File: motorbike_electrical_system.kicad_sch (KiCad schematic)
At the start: 94 parts, among them IC1 BDX34C, IC2 BDX34C, IC3 BDX34C, IC4 BDX34C, IC5 BDX34C, IC6 BDX34C, U1 L7805, U2 L7805, U3 L7805

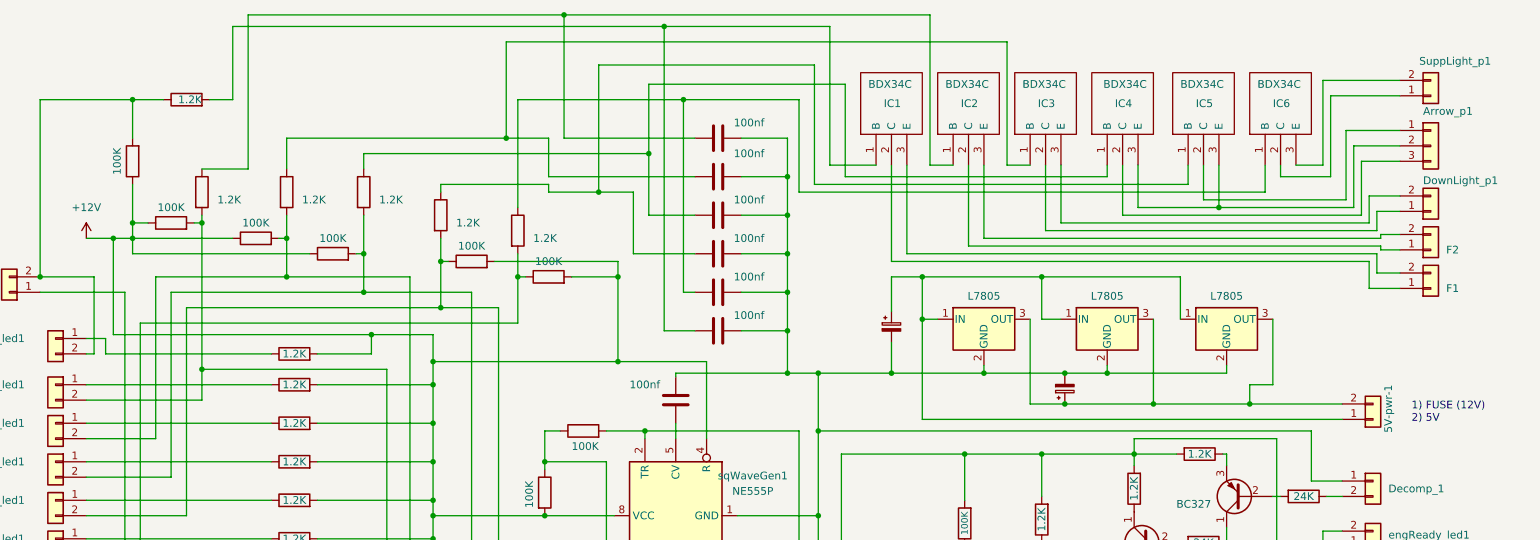
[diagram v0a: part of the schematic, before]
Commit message: enhancement: BDX34C replaced by D45VH10
In order to reduce the wasted electric power BDX34C (VCE=2.5V) has been replaced by D45VH10 (VCE=0.3V) for up-light and added-light
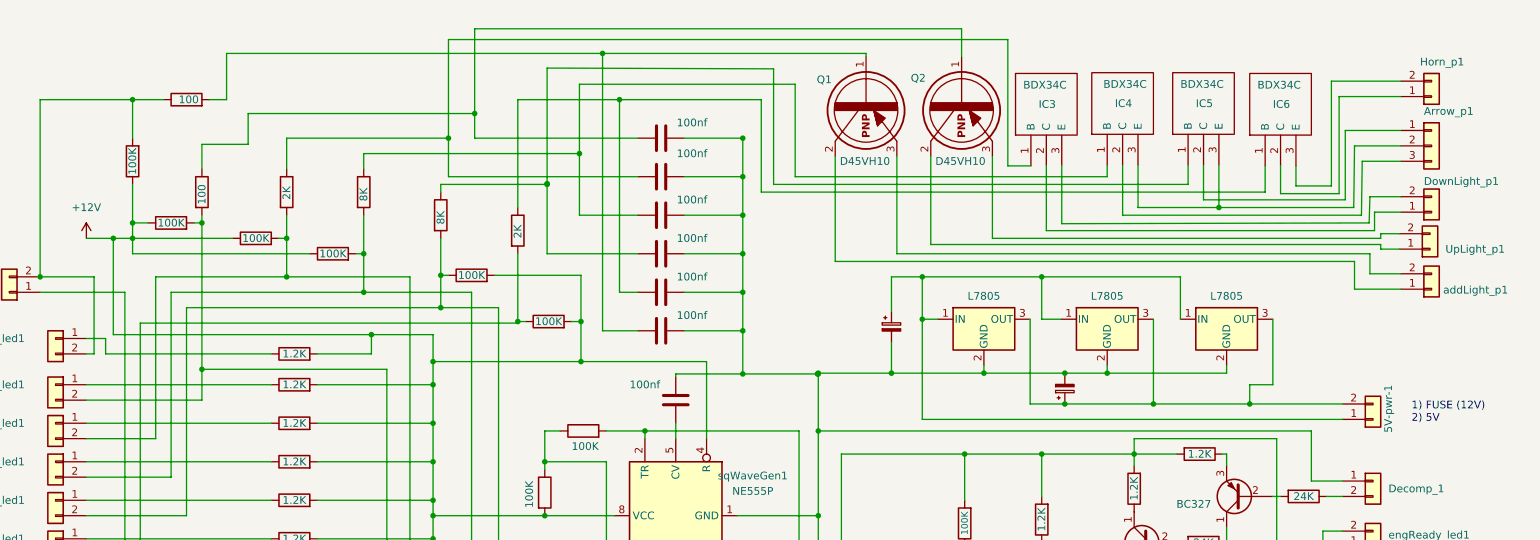
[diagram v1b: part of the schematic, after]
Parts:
- removed IC1, IC2: BDX34C, BDX34C:TO270P460X1020X2008-3P, symbol BDX34C:BDX34C
- added Q1, Q2: D45VH10, Package_TO_SOT_THT:TO-220-3_Vertical, symbol D45VH10:D45VH10
- BT5, RB1, RB2, RB3, RBT2, RBT3, RBT4, RC1, RC2: footprint Resistor_THT:R_Axial_DIN0207_L6.3mm_D2.5mm_P7.62mm_Horizontal -> Resistor_THT:R_Axial_DIN0204_L3.6mm_D1.6mm_P5.08mm_Horizontal
- RBT1, RBT6: footprint Resistor_THT:R_Axial_DIN0207_L6.3mm_D2.5mm_P7.62mm_Horizontal -> Resistor_THT:R_Axial_DIN0204_L3.6mm_D1.6mm_P7.62mm_Horizontal
- RTA1, RTA6: value 1.2K -> 100; footprint Resistor_THT:R_Axial_DIN0207_L6.3mm_D2.5mm_P7.62mm_Horizontal -> Resistor_THT:R_Axial_DIN0516_L15.5mm_D5.0mm_P20.32mm_Horizontal
- RTA2, RTA5: value 1.2K -> 2K
- RTA3, RTA4: value 1.2K -> 8K; footprint Resistor_THT:R_Axial_DIN0207_L6.3mm_D2.5mm_P7.62mm_Horizontal -> Resistor_THT:R_Axial_DIN0204_L3.6mm_D1.6mm_P7.62mm_Horizontal
- renumbered SuppLight_p1 to Horn_p1, F2 to UpLight_p1, F1 to addLight_p1
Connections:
- net at C8.1, RTA6.2: now also Q1.1
- net at C3.1, RTA1.1: now also Q2.1
- net at UpLight_p1.1 (Pin_1): now also Q2.2
- net at UpLight_p1.2 (Pin_2): now also Q2.3
- net at addLight_p1.1 (Pin_1): now also Q1.2
- net at addLight_p1.2 (Pin_2): now also Q1.3

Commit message: First release of all-in-one solution
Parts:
- removed 12V-keyON1, Batt_12V1: Conn_01x01, Connector_Wire:SolderWire-0.5sqmm_1x01_D0.9mm_OD2.1mm, symbol Connector_Generic:Conn_01x01
- removed 5V-pwr-1, DownLight_p1, Horn_p1, UpLight_p1, addLight_p1: Conn_01x02, Connector_Wire:SolderWire-1.5sqmm_1x02_P6mm_D1.7mm_OD3mm, symbol Connector_Generic:Conn_01x02
- removed Arrow_p1: Conn_01x03, Connector_Wire:SolderWire-1.5sqmm_1x03_P6mm_D1.7mm_OD3mm, symbol Connector_Generic:Conn_01x03
- removed BT5, RB1, RB2, RB3, RBT2, RBT3, RBT4, RC1, RC2: 100K, Resistor_THT:R_Axial_DIN0204_L3.6mm_D1.6mm_P5.08mm_Horizontal, symbol Device:R
- removed Batt_GND1: Conn_01x01, Connector_Wire:SolderWire-1.5sqmm_1x01_D1.7mm_OD3.9mm, symbol Connector_Generic:Conn_01x01
- removed Bike_stand1, Decomp_1, Decomp_disabl_1, LightOnOff_sw1, addLights1: Conn_01x02, Connector_PinSocket_2.54mm:PinSocket_1x02_P2.54mm_Vertical, symbol Connector_Generic:Conn_01x02
- removed C1: 1uF, Capacitor_THT:CP_Radial_D6.3mm_P2.50mm, symbol Device:C
- removed C10: C_Polarized_Small, Capacitor_THT:CP_Radial_D8.0mm_P2.50mm, symbol Device:C_Polarized_Small
- removed C11, C12, C13: 50uF, Capacitor_THT:CP_Radial_D6.3mm_P2.50mm, symbol Device:C
- removed C2, C3, C4, C5, C6, C7, C8: 100nf, Capacitor_THT:C_Disc_D6.0mm_W4.4mm_P5.00mm, symbol Device:C
- removed DC1: BC327, Package_TO_SOT_THT:TO-92_Inline_Wide, symbol Transistor_BJT:BC327
- removed DC2, DC3, DC4, DC5, Q_arr1, Q_arr2: BC337, Package_TO_SOT_THT:TO-92_Inline_Wide, symbol Transistor_BJT:BC337
- removed ElectronicKey1: Conn_01x03, Connector_PinHeader_2.54mm:PinHeader_1x03_P2.54mm_Vertical, symbol Connector_Generic:Conn_01x03
- removed GND-faston1: Conn_01x01, Connector_Wire:SolderWire-0.75sqmm_1x01_D1.25mm_OD2.3mm, symbol Connector_Generic:Conn_01x01
- removed GND2DEVS1: Conn_01x06, Connector_Wire:SolderWire-1sqmm_1x06_P7.8mm_D1.4mm_OD3.9mm, symbol Connector_Generic:Conn_01x06
- removed IC3, IC4, IC5, IC6: BDX34C, BDX34C:TO270P460X1020X2008-3P, symbol BDX34C:BDX34C
- removed Q1, Q2: D45VH10, Package_TO_SOT_THT:TO-220-3_Vertical, symbol D45VH10:D45VH10
- removed RA1, RA2, RE1: 5K, Resistor_THT:R_Axial_DIN0207_L6.3mm_D2.5mm_P7.62mm_Horizontal, symbol Device:R
- removed RA3, RA5: 12K, Resistor_THT:R_Axial_DIN0207_L6.3mm_D2.5mm_P7.62mm_Horizontal, symbol Device:R
- removed RA4, RA6, RA8: 24K, Resistor_THT:R_Axial_DIN0207_L6.3mm_D2.5mm_P7.62mm_Horizontal, symbol Device:R
- removed RA7, RL1, RL10, RL2, RL3, RL4, RL5, RL6, RL7, RL8, RL9: 1.2K, Resistor_THT:R_Axial_DIN0207_L6.3mm_D2.5mm_P7.62mm_Horizontal, symbol Device:R
- removed RBT1, RBT6: 100K, Resistor_THT:R_Axial_DIN0204_L3.6mm_D1.6mm_P7.62mm_Horizontal, symbol Device:R
- removed RTA1, RTA6: 100, Resistor_THT:R_Axial_DIN0516_L15.5mm_D5.0mm_P20.32mm_Horizontal, symbol Device:R
- removed RTA2, RTA5: 2K, Resistor_THT:R_Axial_DIN0207_L6.3mm_D2.5mm_P7.62mm_Horizontal, symbol Device:R
- removed RTA3, RTA4: 8K, Resistor_THT:R_Axial_DIN0204_L3.6mm_D1.6mm_P7.62mm_Horizontal, symbol Device:R
- removed RearDevs1: Conn_01x09, Connector_PinHeader_2.54mm:PinHeader_1x09_P2.54mm_Vertical, symbol Connector_Generic:Conn_01x09
- removed addLight_led1, downLight_led1, engReady_led1, engineON_led1, leftArrow_led1, neutralG_led1, rightArrow_led1, upLight_led1: Conn_01x02, Connector_JST:JST_XH_B2B-XH-AM_1x02_P2.50mm_Vertical, symbol Connector_Generic:Conn_01x02
- removed lerftCtrls_conn1, rightCtrls_conn1: Conn_01x06, Connector_PinHeader_2.54mm:PinHeader_1x06_P2.54mm_Vertical, symbol Connector_Generic:Conn_01x06
- removed sqWaveGen1: NE555P, Package_DIP:DIP-8_W7.62mm, symbol Timer:NE555P
- added Battery1: Conn_01x02, Connector_Wire:SolderWire-0.75sqmm_1x02_P7mm_D1.25mm_OD3.5mm, symbol Connector_Generic:Conn_01x02
- added U4: ATmega16L-8P, Package_DIP:DIP-40_W15.24mm, symbol ATmega:ATmega16L-8P
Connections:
- net +12V: now also C9.1, U1.1 (IN), U2.1 (IN), U3.1 (IN), Battery1.1 (Pin_1)
- net GND: now also Battery1.2 (Pin_2), U4.11 (GND), U4.31 (GND)
- net +5V: now reaches U1.3 (OUT), U2.3 (OUT), U3.3 (OUT)
- new net i_Vx1: U4.40 (PA0)
- new net i_Vx2: U4.39 (PA1)
- new net i_addLight: U4.28 (PC6)
- new net i_brakeSwitch: U4.22 (PC0), U4.34 (PA6)
- new net i_bykeStand: U4.6 (PB5)
- new net i_decompr: U4.25 (PC3)
- new net i_downLight: U4.2 (PB1)
- new net i_engineON: U4.24 (PC2)
- new net i_horn: U4.5 (PB4)
- new net i_leftArrow: U4.1 (PB0)
- new net i_lightON/OFF: U4.29 (PC7)
- new net i_neutral: U4.33 (PA7)
- new net i_rightArrow: U4.4 (PB3)
- new net i_startButton: U4.23 (PC1)
- new net i_upLight: U4.3 (PB2)
- new net o_addLight: U4.18 (PD4)
- new net o_downLight: U4.16 (PD2)
- new net o_engineReady: U4.7 (PB6)
- new net o_horn: U4.19 (PD5)
- new net o_keepAlive: U4.20 (PD6)
- new net o_leftArrow: U4.15 (PD1)
- new net o_neutral: U4.8 (PB7)
- new net o_rightArrow: U4.14 (PD0)
- new net o_startEngine: U4.21 (PD7)
- new net o_stopLight: U4.27 (PC5)
- new net o_upLight: U4.17 (PD3)
- new net tempPower: U4.10 (VCC)
- no-connect marks 2 -> 10
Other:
- added sheet MB Electrical System - front outputs (mbes_front_outputs.kicad_sch)
- added sheet MB Electrical System - inputs (mbes_inputs.kicad_sch)
- added sheet MB Electrical System - rear side connector (mbes_rear_connector.kicad_sch)
- note removed: "1) FUSE (12V) 2) 5V"
- note removed: "1) Rear light 2) Left arrow 3) Right arrow 4) STOP light 5) Rear brake 6) START relay 7) Neutral gear 8) Eng-off CDI 9) NC"
- note removed: "1) Square Wave (gray) 2) Left arrow (light blue) 3) DOWN light (white) 4) UP Light (blue) 5) Right Arrow (orange) 6) Horn (verde)"
- note removed: "1) Start butt. (orange) 2) GND (blue) 3) Brake sw. (light blue) 4) Start butt. (black/white) 5) Engine OFF (black) 6) Engine ON (yellow/black)"

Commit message: fix: duplicated signal
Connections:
- net i_brakeSwitch: no longer U4.34 (PA6)
- no-connect marks 10 -> 11
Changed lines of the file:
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@@
   (no_connect (at 112.141 54.102))
   (no_connect (at 142.621 59.182))
+  (no_connect (at 142.6464 69.342))
   (no_connect (at 142.621 64.262))
-  (wire (pts (xy 149.479 68.453) (xy 149.479 69.342))
-    (stroke (width 0) (type default) (color 0 0 0 0))
-  )
   (wire (pts (xy 159.512 82.042) (xy 159.512 83.566))
     (stroke (width 0) (type default) (color 0 0 0 0))
@@
     (stroke (width 0) (type default) (color 0 0 0 0))
   )
-  (wire (pts (xy 149.479 69.342) (xy 142.621 69.342))
-    (stroke (width 0) (type default) (color 0 0 0 0))
-  )
   (wire (pts (xy 153.289 102.362) (xy 142.621 102.362))
     (stroke (width 0) (type default) (color 0 0 0 0))
@@
   )
   (wire (pts (xy 142.621 71.882) (xy 161.417 71.882))
-    (stroke (width 0) (type default) (color 0 0 0 0))
-  )
-  (wire (pts (xy 161.417 68.453) (xy 149.479 68.453))
     (stroke (width 0) (type default) (color 0 0 0 0))
   )
@@
       (effects (font (size 1.27 1.27)) (justify left) hide)
     )
-  )
-  (global_label "i_brakeSwitch" (shape input) (at 161.417 68.453 0) (fields_autoplaced)
-    (effects (font (size 1.27 1.27)) (justify left))
-    (property "Riferimenti inter-foglio" "${INTERSHEET_REFS}" (id 0) (at 176.7115 68.3736 0)
-      (effects (font (size 1.27 1.27)) (justify left) hide)
-    )

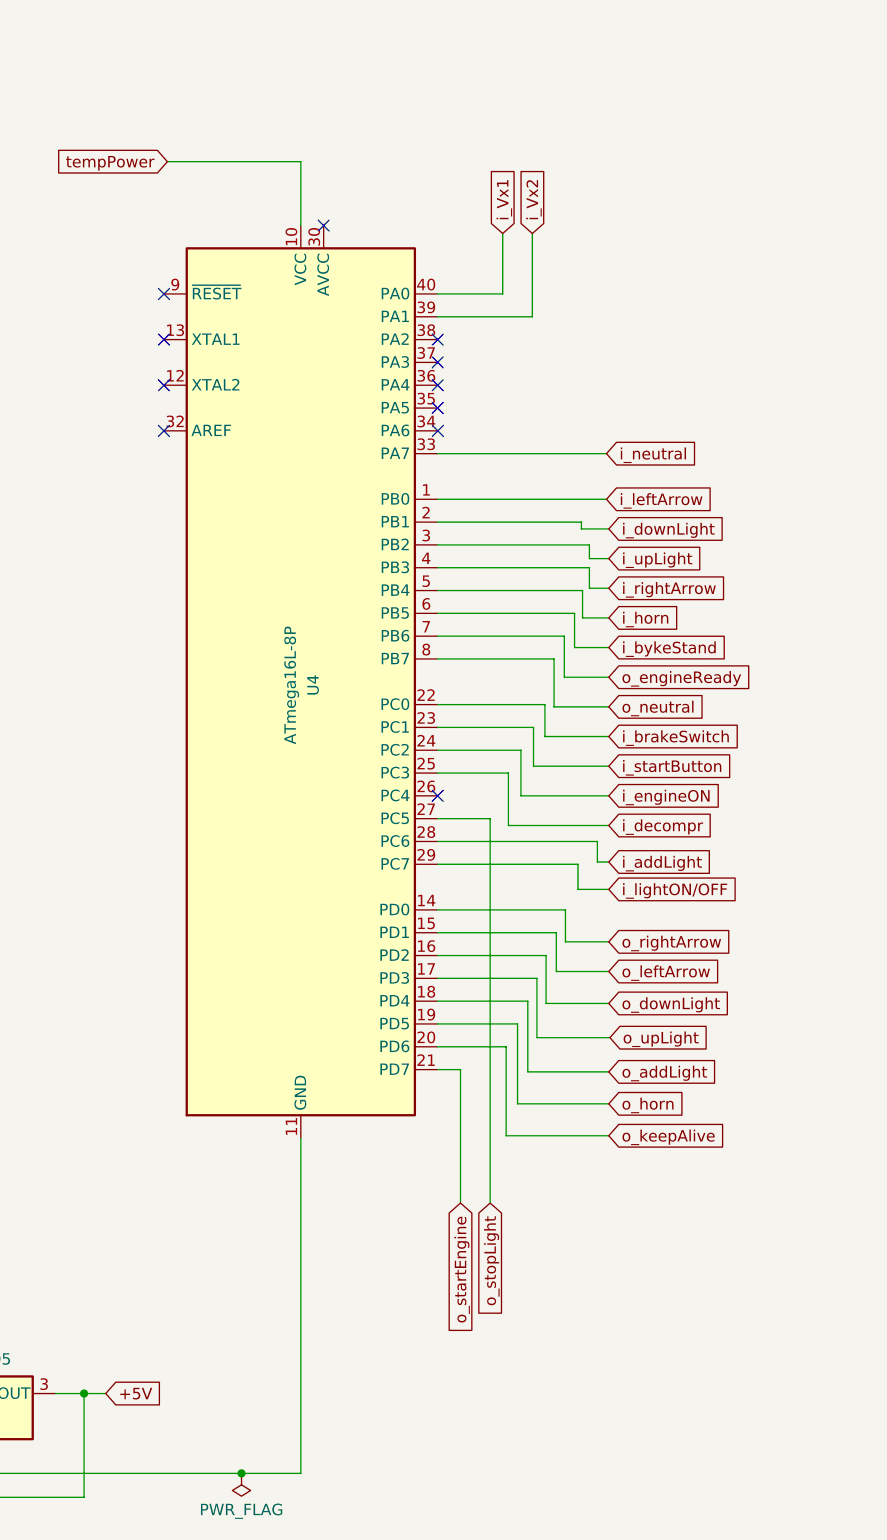
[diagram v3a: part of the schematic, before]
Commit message: fix: missing Vy(1,2) references for the key authentication
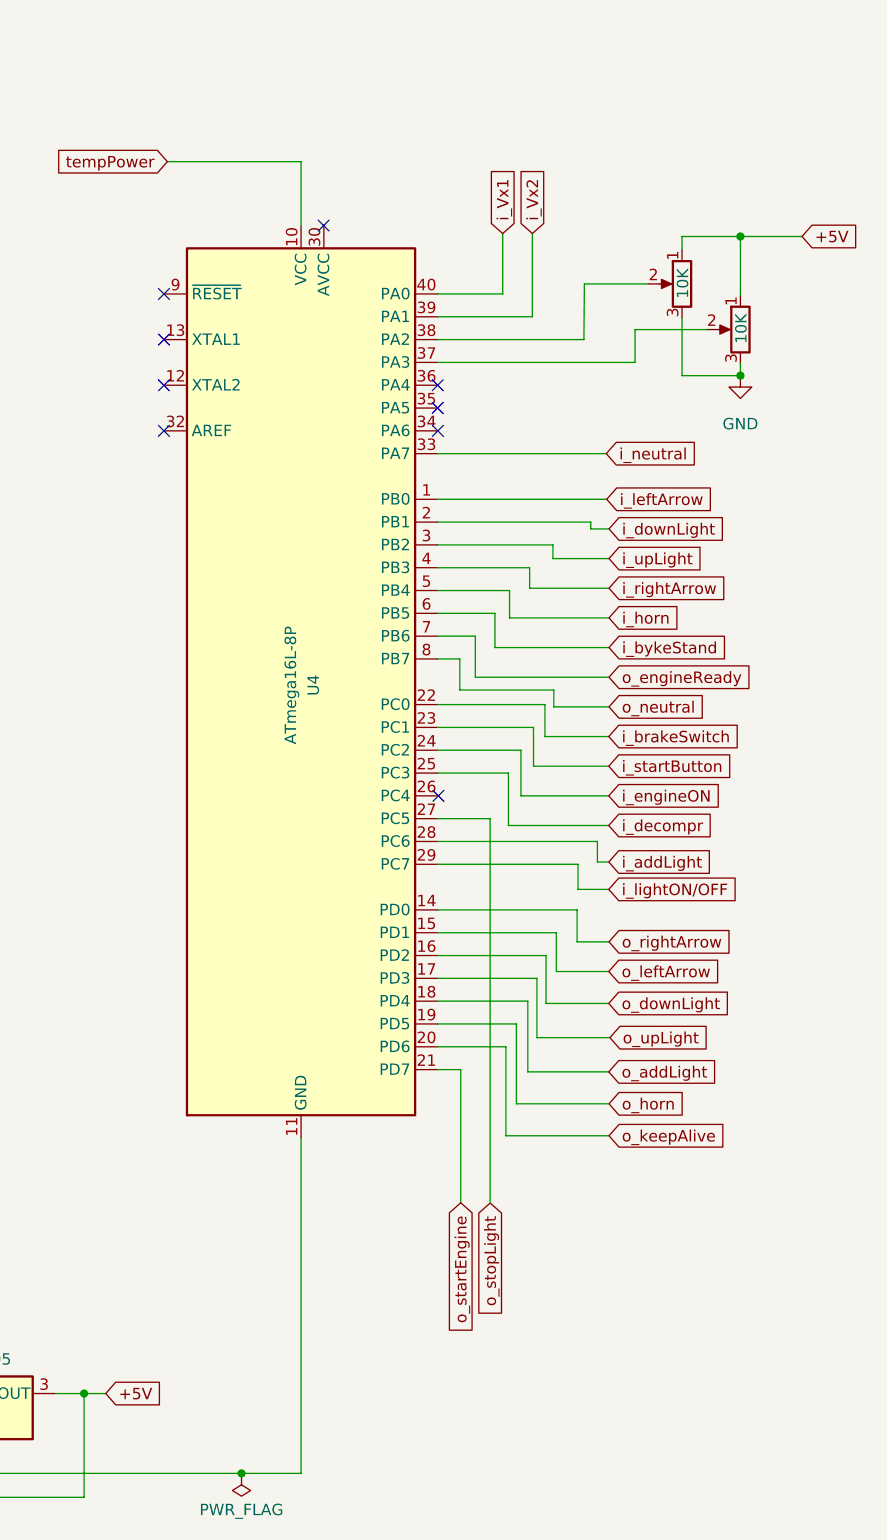
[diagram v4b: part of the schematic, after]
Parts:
- added RV1, RV2: 10K, Potentiometer_THT:Potentiometer_Bourns_3296W_Vertical, symbol Device:R_Potentiometer
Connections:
- net +5V: now also RV1.1, RV2.1
- net GND: now also RV1.3, RV2.3
- net at U4.37 (PA3): now also RV2.2
- net at U4.38 (PA2): now also RV1.2
- no-connect marks 11 -> 9
